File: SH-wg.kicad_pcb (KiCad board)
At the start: 4 copper layers, 54.6 x 99.2 mm, 85 parts, among them J101 Aux PCB Conn Male, J102 Aux PCB Conn Female, J201 Conn_01x05, J301 JTAG, J302 Digital IO, J303 Analog IO, J401 Power, J501 Conn_01x04, J701 Conn_02x03_Odd_Even, Q801 2N7002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

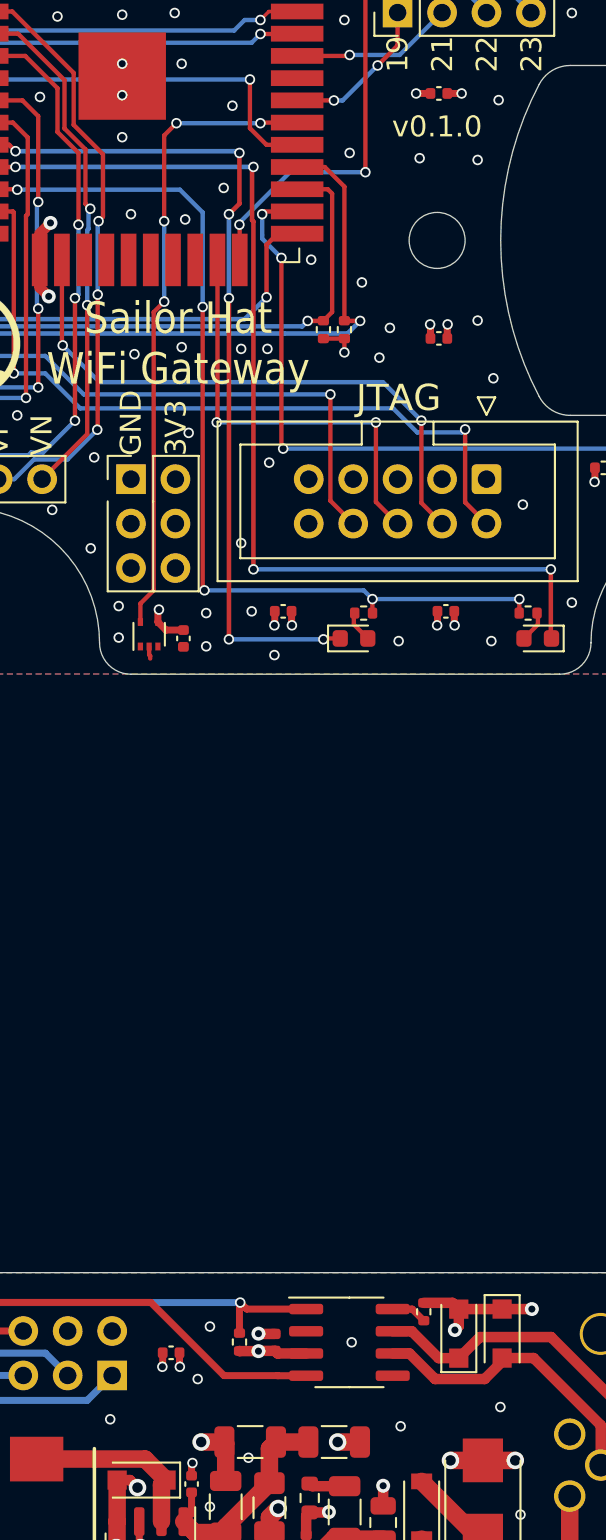
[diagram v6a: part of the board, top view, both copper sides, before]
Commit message: Bump the board version, improve silkscreens
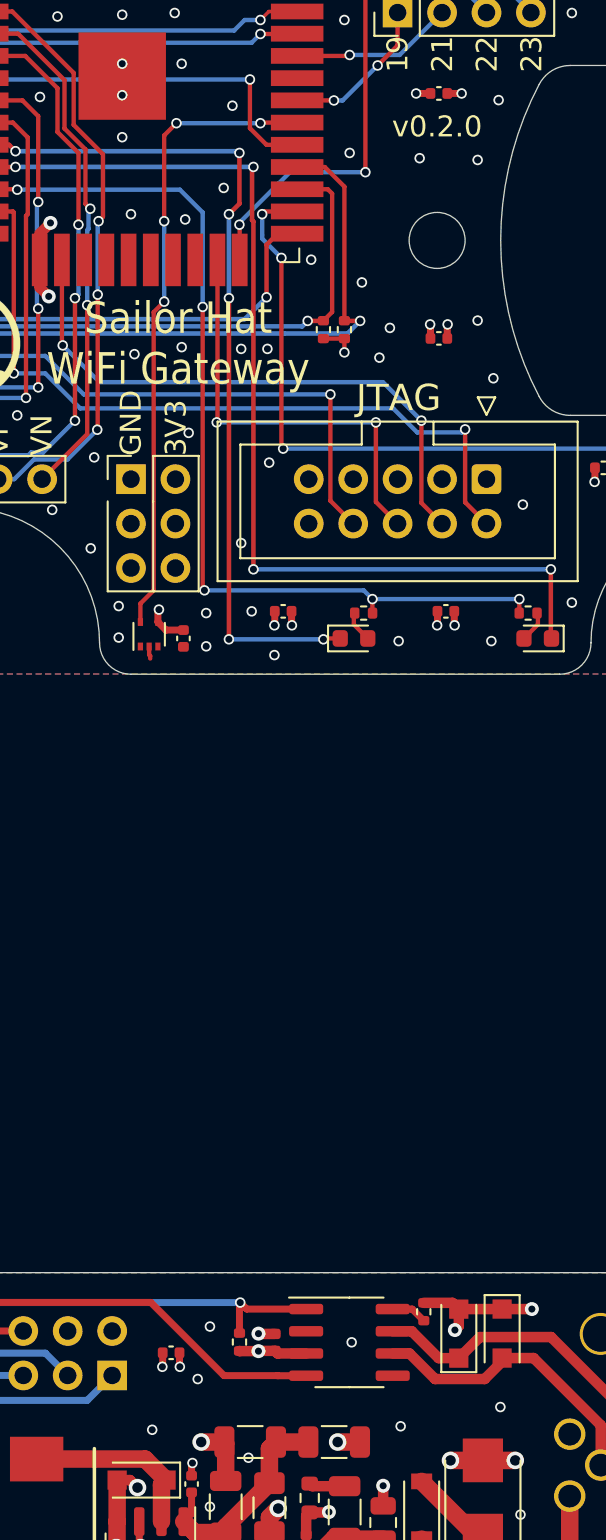
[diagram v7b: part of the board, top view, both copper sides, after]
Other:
- board text added: "12V"
- board text added: "EN"
- board text added: "H"
- board text added: "IO0"
- board text added: "L"
- board text added: "RXD"
- board text added: "TXD"
- board text added: "v0.2.0"
- board text removed: "v0.1.0"
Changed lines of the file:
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@@
   (title_block
     (title "Sailor Hat Wireless Gateway")
-    (date "2022-01-26")
-    (rev "0.1.0")
+    (date "2022-02-23")
+    (rev "0.2.0")
     (company "Hat Labs Ltd")
     (comment 1 "https://creativecommons.org/licenses/by/4.0")
@@
     (effects (font (size 0.8 0.8) (thickness 0.15)) (justify left mirror))
   )
+  (gr_text "12V" (at 87.9 131.2 180) (layer "B.SilkS")
+    (effects (font (size 0.8 0.8) (thickness 0.15)) (justify mirror))
+  )
+  (gr_text "GND" (at 91.5 131.2 180) (layer "B.SilkS")
+    (effects (font (size 0.8 0.8) (thickness 0.15)) (justify mirror))
+  )
+  (gr_text "TXD" (at 59.2 126.3 180) (layer "B.SilkS")
+    (effects (font (size 0.8 0.8) (thickness 0.15)) (justify mirror))
+  )
+  (gr_text "RXD" (at 56.7 126.3 180) (layer "B.SilkS")
+    (effects (font (size 0.8 0.8) (thickness 0.15)) (justify mirror))
+  )
   (gr_text "Sailor Hat\nWiFi Gateway" (at 64.685 123.72 -180) (layer "B.SilkS")
     (effects (font (size 1.8 1.6) (thickness 0.35)) (justify left mirror))
@@
     (effects (font (size 0.8 0.8) (thickness 0.15)) (justify left mirror))
   )
-  (gr_text "v0.1.0" (at 67.685 119.62 180) (layer "B.SilkS")
+  (gr_text "GND" (at 59.2 124.7 180) (layer "B.SilkS")
+    (effects (font (size 0.8 0.8) (thickness 0.15)) (justify mirror))
+  )
+  (gr_text "H" (at 91.4 124 180) (layer "B.SilkS")
+    (effects (font (size 0.8 0.8) (thickness 0.15)) (justify mirror))
+  )
+  (gr_text "v0.2.0" (at 67.685 119.62 180) (layer "B.SilkS")
     (effects (font (size 1.2 1.2) (thickness 0.25)) (justify mirror))
   )
+  (gr_text "L" (at 86.4 127.6 180) (layer "B.SilkS")
+    (effects (font (size 0.8 0.8) (thickness 0.15)) (justify mirror))
+  )
   (gr_text "I2C" (at 51.485 133.92 180) (layer "B.SilkS")
     (effects (font (size 1.2 1.2) (thickness 0.25)) (justify mirror))
   )
+  (gr_text "3V3" (at 61.7 124.7 180) (layer "B.SilkS")
+    (effects (font (size 0.8 0.8) (thickness 0.15)) (justify mirror))
+  )
   (gr_text "GND" (at 52.7 123.82 180) (layer "B.SilkS")
     (effects (font (size 0.8 0.8) (thickness 0.15)) (justify left mirror))
   )
+  (gr_text "EN" (at 61.7 126.3 180) (layer "B.SilkS")
+    (effects (font (size 0.8 0.8) (thickness 0.15)) (justify mirror))
+  )
   (gr_text "Prog" (at 54.885 119.82 180) (layer "B.SilkS")
     (effects (font (size 1.2 1.2) (thickness 0.25)) (justify right mirror))
   )
+  (gr_text "IO0" (at 56.7 124.7 180) (layer "B.SilkS")
+    (effects (font (size 0.8 0.8) (thickness 0.15)) (justify mirror))
+  )
   (gr_text "3V3" (at 52.985 126.32 180) (layer "B.SilkS")
     (effects (font (size 0.8 0.8) (thickness 0.15)) (justify left mirror))
@@
     (effects (font (size 1.2 1.2) (thickness 0.25)) (justify left))
   )
-  (gr_text "v0.1.0" (at 80.285 51.12) (layer "F.SilkS")
+  (gr_text "v0.2.0" (at 80.285 51.12) (layer "F.SilkS")
     (effects (font (size 1.2 1.2) (thickness 0.25)))
   )
@@
   (via (at 85.05 130.45) (size 0.6) (drill 0.4) (layers "F.Cu" "B.Cu") (net 42))
   (via (at 74.6 126.3) (size 1) (drill 0.6) (layers "F.Cu" "B.Cu") (net 42))
-  (via (at 61.6 125) (size 0.6) (drill 0.4) (layers "F.Cu" "B.Cu") (free) (net 42))
+  (via (at 64 125.6) (size 0.6) (drill 0.4) (layers "F.Cu" "B.Cu") (free) (net 42))
   (via (at 86.7 135.9) (size 0.6) (drill 0.4) (layers "F.Cu" "B.Cu") (free) (net 42))
   (via (at 84.75 127.35) (size 1) (drill 0.6) (layers "F.Cu" "B.Cu") (net 42))

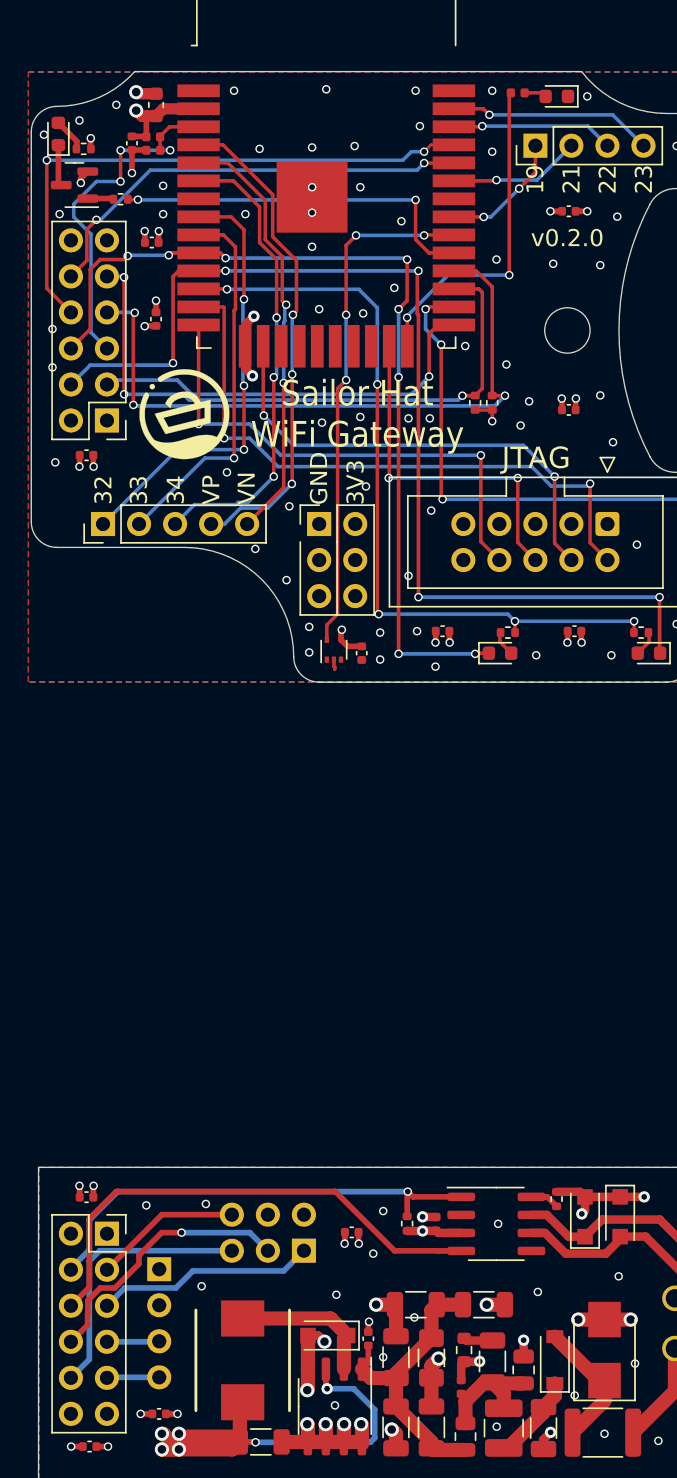
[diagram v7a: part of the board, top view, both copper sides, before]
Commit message: Update LED resistor values, improve PCB edge clearance
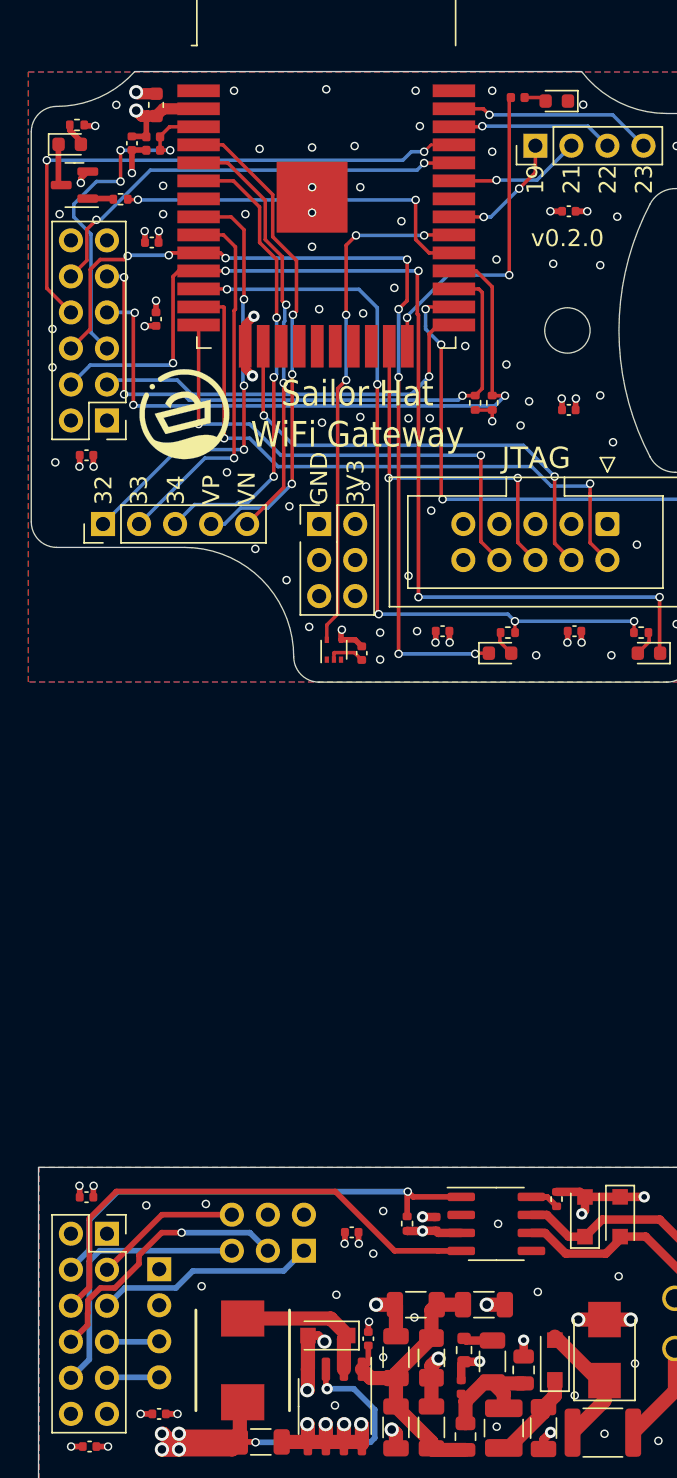
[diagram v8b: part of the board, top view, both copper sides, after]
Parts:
- D602: footprint Diode_SMD:D_SOD-123 -> Diode_SMD:D_SOD-123F
- R802: value 1.5k -> 1.0k
- R803, R804: value 2k -> 1.5k
- R806: value 2.2k -> 2k
- moved R806 1.75 mm to (45.7, 43.1)
- moved D805 1.08 mm to (45.2, 44.5), turned to 0 degrees
- moved D802 0.33 mm to (79.5, 41.5)
- moved R802 0.33 mm to (76.8, 41.2)
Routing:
- net GND: track 17.8 -> 19.7 mm, vias 76 -> 72
- net Net-(D805-Pad2): track 2.38 -> 1.69 mm
